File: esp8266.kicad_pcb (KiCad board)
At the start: 2 copper layers, 55.1 x 26 mm, 47 parts, among them J1 Conn_01x08, J2 Conn_01x08, Q1 AO3401A, U10 RST, U11 W25Q128JVSIQTR, U13 CH340C, U2 ESP8266EX, U3 AP2112K-3_3TRG1, U4 HDC1080DMBR, U5 MCP73831T-2ACI_OT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

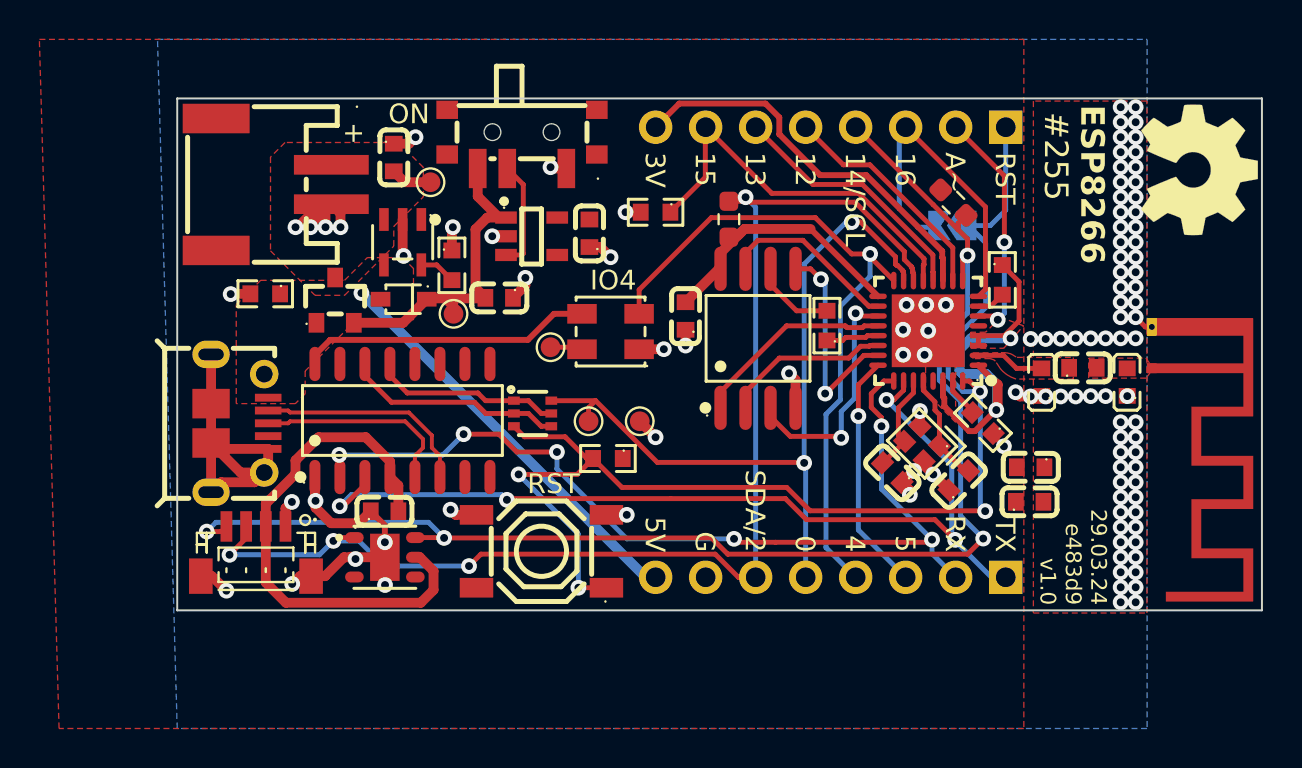
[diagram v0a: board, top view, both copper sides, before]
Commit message: Rework layout to retain power and ground plane continuity.
Add one more decoupling capacitor to CH340.

The ground plane now has islands of shorter traces. The 3.3V plane has been carefully adjusted to provide reasonable impedances to all loads.
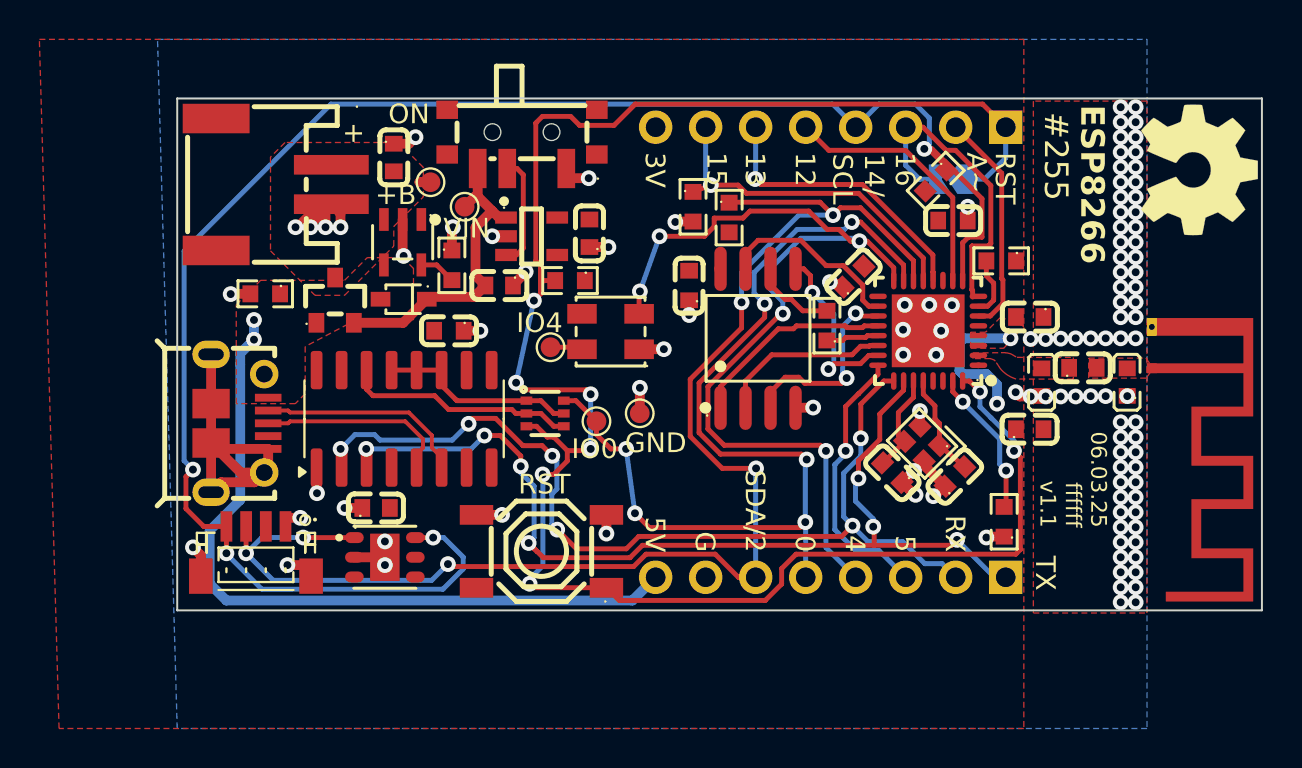
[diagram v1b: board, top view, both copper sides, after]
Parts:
- added C11: 100n, jlc_footprints:C0603, F.Cu at (97.4, 129.2)
- added C14: 100n, jlc_footprints:C0603, F.Cu at (84.0, 132.5)
- added C15: 100n, jlc_footprints:C0603, F.Cu at (71.8, 134.8)
- R8, R9: footprint Resistor_SMD:R_0603_1608Metric_Pad0.98x0.95mm_HandSolder -> jlc_footprints:R0603
- U13: footprint jlc_footprints:SOP-16_L10.0-W3.9-P1.27-LS6.0-BL -> Package_SO:SOIC-16_3.9x9.9mm_P1.27mm
- moved R5 9.24 mm to (78.0, 132.2)
- moved C10 8.76 mm to (92.3, 132.1), turned to 45 degrees
- moved C2 7.63 mm to (101.3, 134.1)
- moved TP6 5.47 mm to (72.6, 128.5)
- moved R1 5.13 mm to (100.0, 144.5), turned to 90 degrees
- moved C1 3.69 mm to (101.3, 139.8)
- moved JP2 2.36 mm to (97.4, 127.1)
- moved R6 1.92 mm to (84.2, 128.5), turned to -90 degrees
- moved R9 1.44 mm to (96.5, 127.2), turned to -135 degrees
- moved R3 0.97 mm to (99.8, 131.2), turned to 180 degrees
- moved U9 0.64 mm to (76.7, 139.0)
- moved C7 0.63 mm to (74.4, 132.5)
- moved C8 0.46 mm to (68.1, 143.8)
- moved TP5 0.40 mm to (81.5, 139.0)
- moved TP4 0.40 mm to (79.3, 139.4)
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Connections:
- U13 pad 10: unconnected-(U13-~{DSR}-Pad10) -> +3V3
- U13 pad 11: unconnected-(U13-~{RI}-Pad11) -> DTR
- U13 pad 12: unconnected-(U13-~{DCD}-Pad12) -> DTR
- U13 pad 9: unconnected-(U13-~{CTS}-Pad9) -> +3V3
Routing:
- net +3V3: track 96.9 -> 7.36 mm
- net RESET: track 62.9 -> 98.7 mm, vias 4 -> 8
- net GPIO14: track 70.2 -> 88.3 mm
- net VBUS: track 20.9 -> 37.8 mm, vias 1 -> 2
- net GPIO4: track 35.1 -> 47.4 mm, vias 1 -> 5
- net GND: track 69.4 -> 59.2 mm, vias 110 -> 113
- net GPIO0: track 38.9 -> 49.1 mm, vias 2 -> 6
- net GPIO2: track 62.5 -> 71.5 mm, vias 4 -> 6
- net Net-(U2-RES12K): track 2.02 -> 7.57 mm, vias 0 -> 2
- net LNA: track 3.49 -> 0.00 mm
- net GPIO15: track 20.0 -> 17.5 mm, vias 0 -> 1
- net U0TXD: track 48.1 -> 50.4 mm, vias 4 -> 7
- net SD_WP: track 12.3 -> 10.1 mm
- net SD_SI: track 10.9 -> 9.06 mm
- net U0RXD: track 47.0 -> 48.8 mm
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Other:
- board text added: "06.03.25 ffffff v1.1"
- board text added: "14/ SCL"
- board text removed: "14/SCL"
- board text removed: "29.03.24 e483d9 v1.0"
- board text removed: "IO4"
